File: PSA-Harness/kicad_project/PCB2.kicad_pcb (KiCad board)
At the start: 4 copper layers, 28.3 x 54 mm, 15 parts, among them J1 to_EPS_1, J2 to_EPS_2, J3 to_ESP_3, J7 USB_C_Receptacle, J8 B2B_1, J9 B2B_2, U1 DG419LEUA, U2 DG419LEUA

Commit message: use bom component names
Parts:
- D1, D2: value BAS40TW-AU -> BAS40SDW-AU_R1_000A1
- J7: value USB_C_Receptacle -> TYPE-C-31-M-07
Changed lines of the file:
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@@
 			)
 		)
-		(property "Value" "USB_C_Receptacle"
-			(at -0.6 -3.835 270)
+		(property "Value" "TYPE-C-31-M-07"
+			(at -0.6 -3.835 90)
 			(layer "F.Fab")
 			(effects
@@
 		(tags "SOT-363 SC-70-6 SC-88")
 		(property "Reference" "D1"
-			(at 0 2.03 270)
+			(at 0 2.03 90)
 			(layer "F.SilkS")
 			(effects
@@
 			)
 		)
-		(property "Value" "BAS40TW-AU"
-			(at 0 2 270)
+		(property "Value" "BAS40SDW-AU_R1_000A1"
+			(at 0 2 90)
 			(layer "F.Fab")
 			(effects
@@
 		)
 		(fp_text user "${REFERENCE}"
-			(at 0 0 180)
+			(at 0 0 0)
 			(layer "F.Fab")
 			(effects
@@
 			)
 		)
-		(property "Value" "BAS40TW-AU"
+		(property "Value" "BAS40SDW-AU_R1_000A1"
 			(at 0 2 90)
 			(layer "F.Fab")

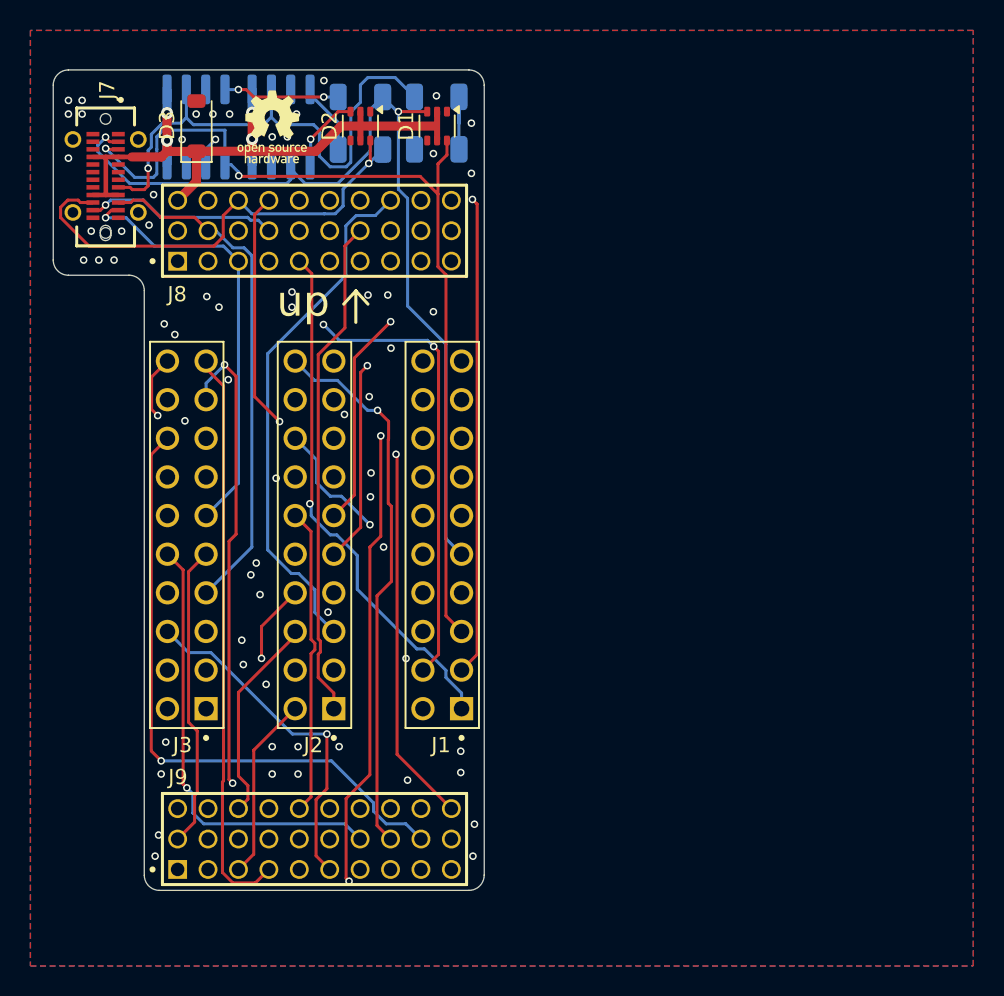
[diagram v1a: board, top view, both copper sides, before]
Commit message: move all psa harness components to top layer
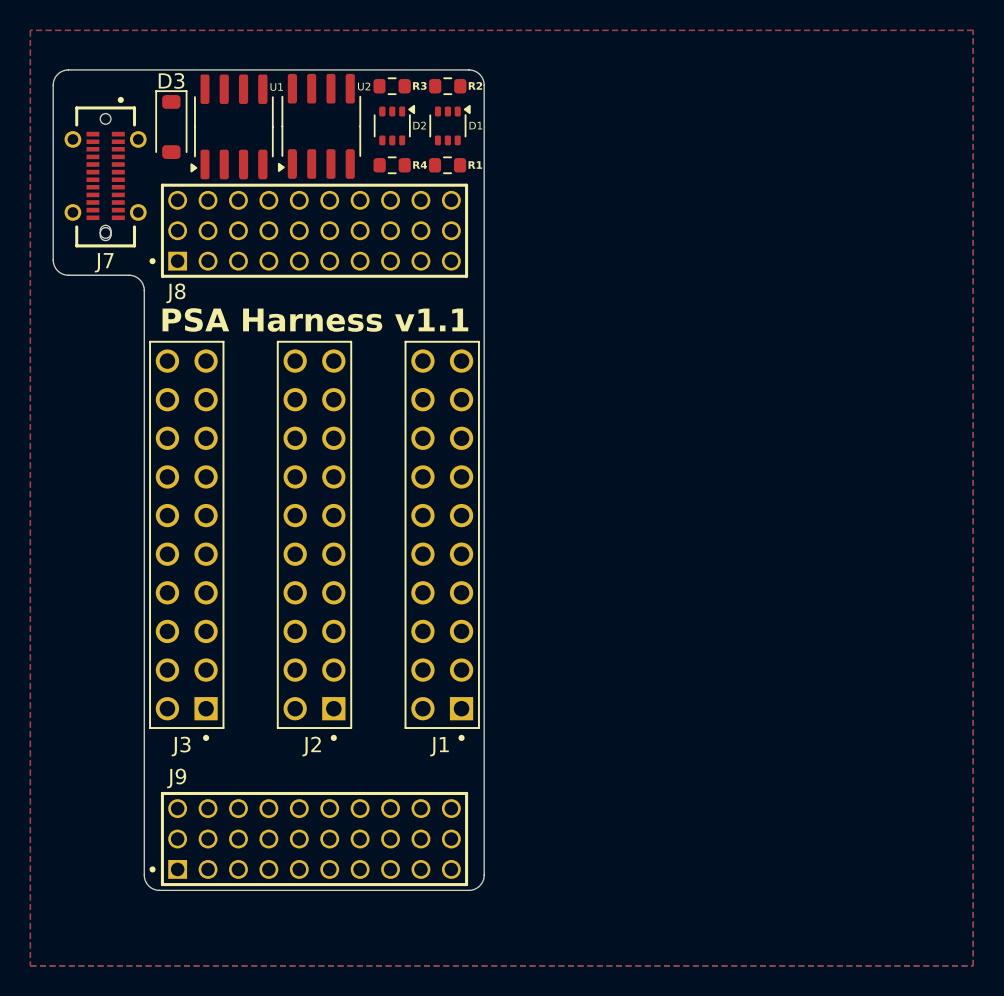
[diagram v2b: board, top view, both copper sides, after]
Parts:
- R1, R2, R3, R4: footprint Resistor_SMD:R_1206_3216Metric -> Resistor_SMD:R_0603_1608Metric; moved to F.Cu
- U1, U2: moved to F.Cu
- moved R1 5.82 mm to (114.4, 97.9), turned to 0 degrees
- moved R2 5.79 mm to (114.4, 92.7), turned to 180 degrees
- moved R4 3.11 mm to (110.8, 97.9), turned to 0 degrees
- moved R3 3.02 mm to (110.8, 92.7), turned to 180 degrees
- moved U2 2.65 mm to (106.1, 95.3)
- moved U1 2.49 mm to (100.4, 95.3)
- moved D2 2.10 mm to (110.8, 95.3)
- moved D3 1.65 mm to (96.3, 95.4), turned to -90 degrees
- moved D1 0.71 mm to (114.5, 95.3)
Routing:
- net +12V: track 81.5 -> 0.00 mm, vias 4 -> 0
- net CAN0_L: track 62.6 -> 0.00 mm, vias 2 -> 0
- net CAN0_H: track 61.6 -> 0.00 mm, vias 2 -> 0
- net 59: track 47.6 -> 0.00 mm, vias 1 -> 0
- net 60: track 47.4 -> 0.00 mm, vias 2 -> 0
- net 28: track 45.3 -> 0.00 mm, vias 2 -> 0
- net 2: track 43.6 -> 0.00 mm, vias 1 -> 0
- net 12: track 42.1 -> 0.00 mm, vias 2 -> 0
- net 58: track 41.5 -> 0.00 mm, vias 1 -> 0
- net 30: track 38.2 -> 0.00 mm, vias 1 -> 0
- net 56: track 38.0 -> 0.00 mm, vias 1 -> 0
- net CAN2_L: track 38.0 -> 0.00 mm, vias 2 -> 0
- net 50: track 37.8 -> 0.00 mm
- net SBU1: track 37.2 -> 0.00 mm, vias 1 -> 0
- net 29: track 36.2 -> 0.00 mm, vias 1 -> 0
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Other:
- board text added: "PSA Harness v1.1"
- board text removed: "up"

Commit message: CAN signals routed
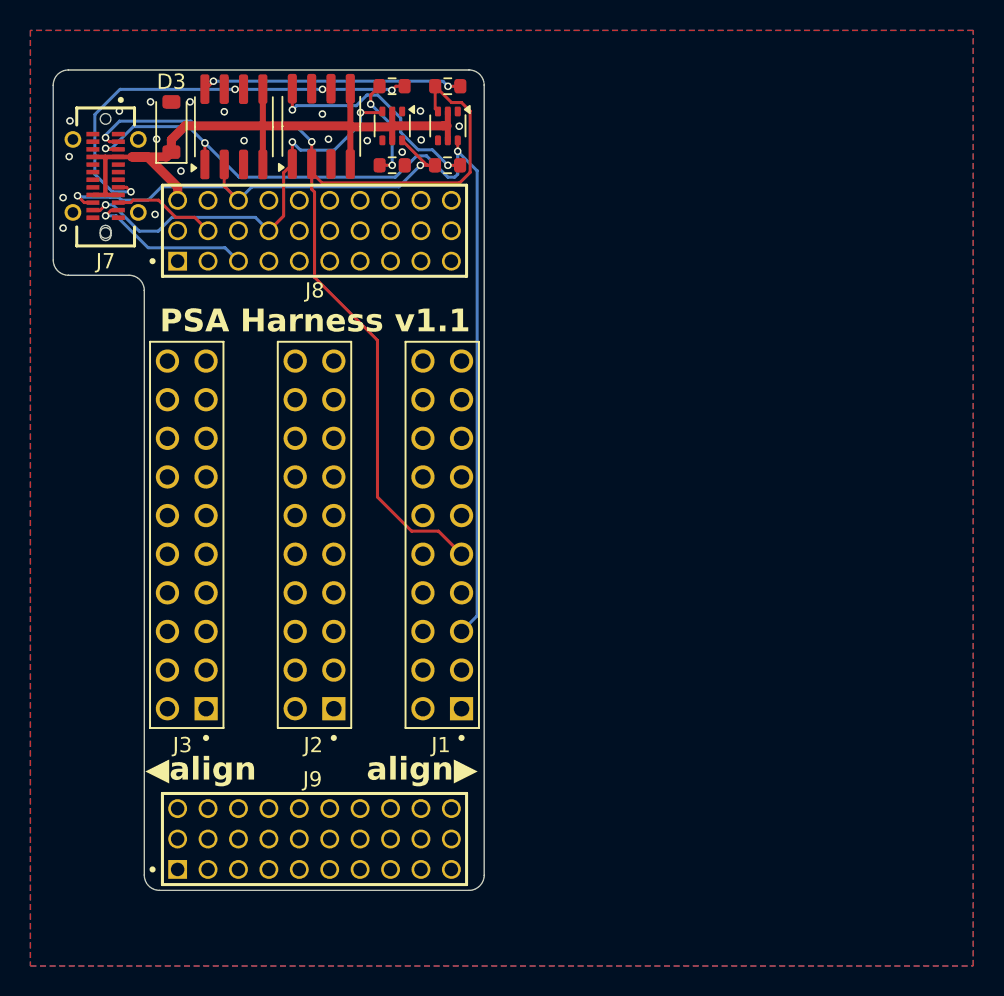
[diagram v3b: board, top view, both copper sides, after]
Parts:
- turned D3 to 90 degrees
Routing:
- net CAN0_H: track 0.00 -> 68.0 mm, vias 0 -> 2
- net CAN0_L: track 0.00 -> 63.4 mm, vias 0 -> 3
- net +12V: track 0.00 -> 47.3 mm
- net CAN2_L: track 0.00 -> 32.1 mm, vias 0 -> 2
- net SBU1: track 0.00 -> 30.1 mm, vias 0 -> 4
- net CAN2_H: track 0.00 -> 27.3 mm, vias 0 -> 3
- net Net-(R2-Pad1): track 0.00 -> 17.2 mm, vias 0 -> 2
- net Net-(R1-Pad2): track 0.00 -> 15.3 mm, vias 0 -> 2
- net CAN1_H: track 0.00 -> 11.0 mm, vias 0 -> 1
- net Net-(R3-Pad2): track 0.00 -> 6.85 mm, vias 0 -> 2
- net CAN1_L: track 0.00 -> 6.80 mm
- net GND: vias 0 -> 19
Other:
- board text added: "align▶"
- board text added: "◀align"

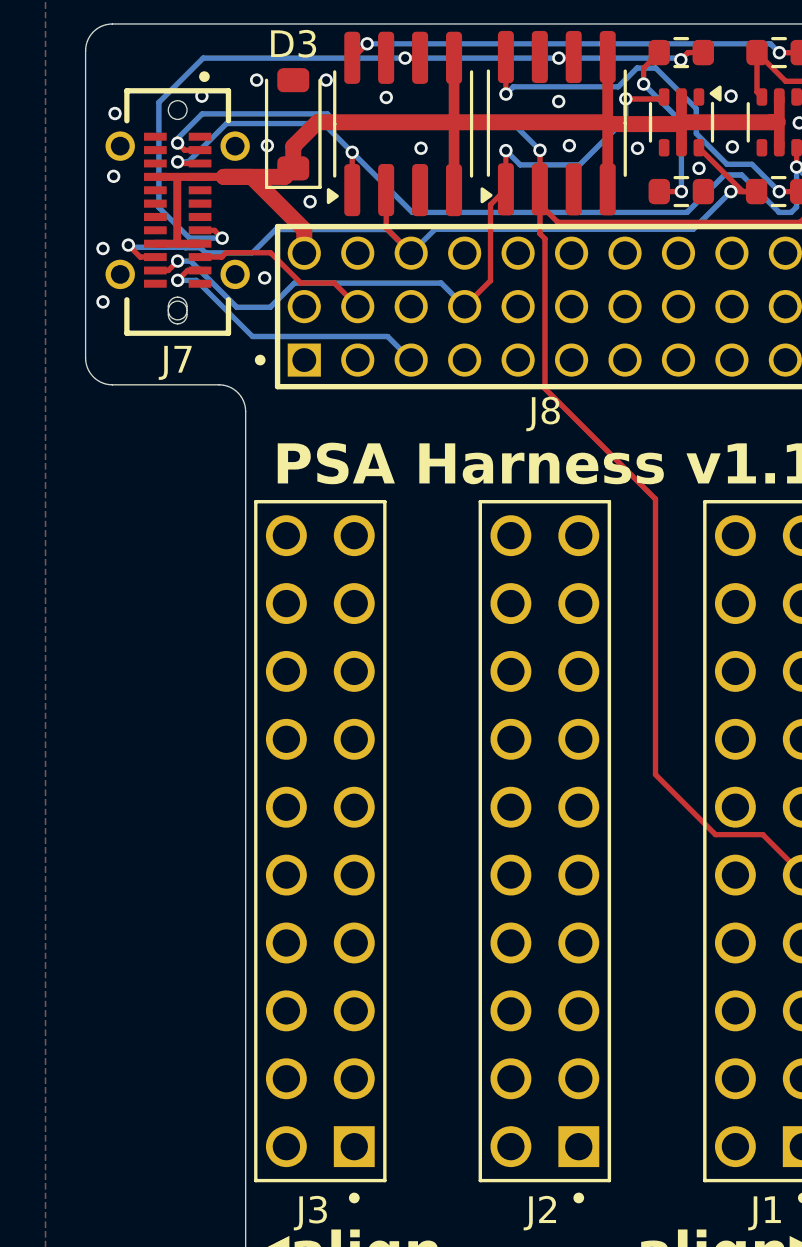
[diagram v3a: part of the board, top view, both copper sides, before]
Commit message: routed power
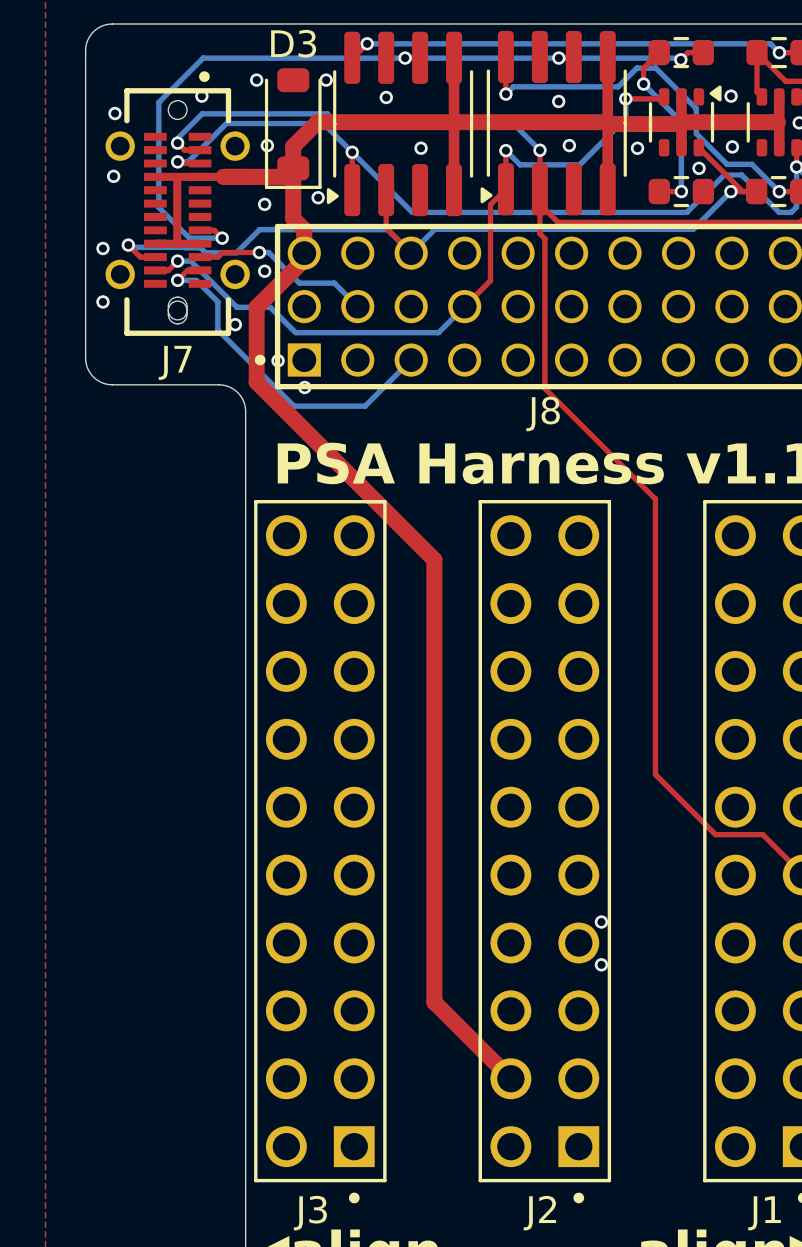
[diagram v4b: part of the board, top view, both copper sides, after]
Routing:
- net +12V: track 47.3 -> 82.6 mm
- net CAN1_H: track 11.0 -> 13.0 mm
- net CAN1_L: track 6.80 -> 6.81 mm, vias 0 -> 1
- net GND: vias 19 -> 25

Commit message: pcb2 routed
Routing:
- net 59: track 0.00 -> 51.7 mm
- net 21: track 0.00 -> 44.1 mm, vias 0 -> 2
- net 2: track 0.00 -> 43.5 mm, vias 0 -> 1
- net 60: track 0.00 -> 43.0 mm, vias 0 -> 1
- net 58: track 0.00 -> 39.5 mm, vias 0 -> 1
- net 12: track 0.00 -> 39.0 mm, vias 0 -> 1
- net 28: track 0.00 -> 38.4 mm, vias 0 -> 1
- net 40: track 0.00 -> 38.3 mm, vias 0 -> 2
- net 14: track 0.00 -> 37.8 mm, vias 0 -> 2
- net 30: track 0.00 -> 37.8 mm, vias 0 -> 1
- net 50: track 0.00 -> 37.5 mm, vias 0 -> 1
- net 57: track 0.00 -> 36.5 mm, vias 0 -> 1
- net 29: track 0.00 -> 35.6 mm, vias 0 -> 1
- net 56: track 0.00 -> 35.5 mm, vias 0 -> 1
- net 1: track 0.00 -> 34.1 mm
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
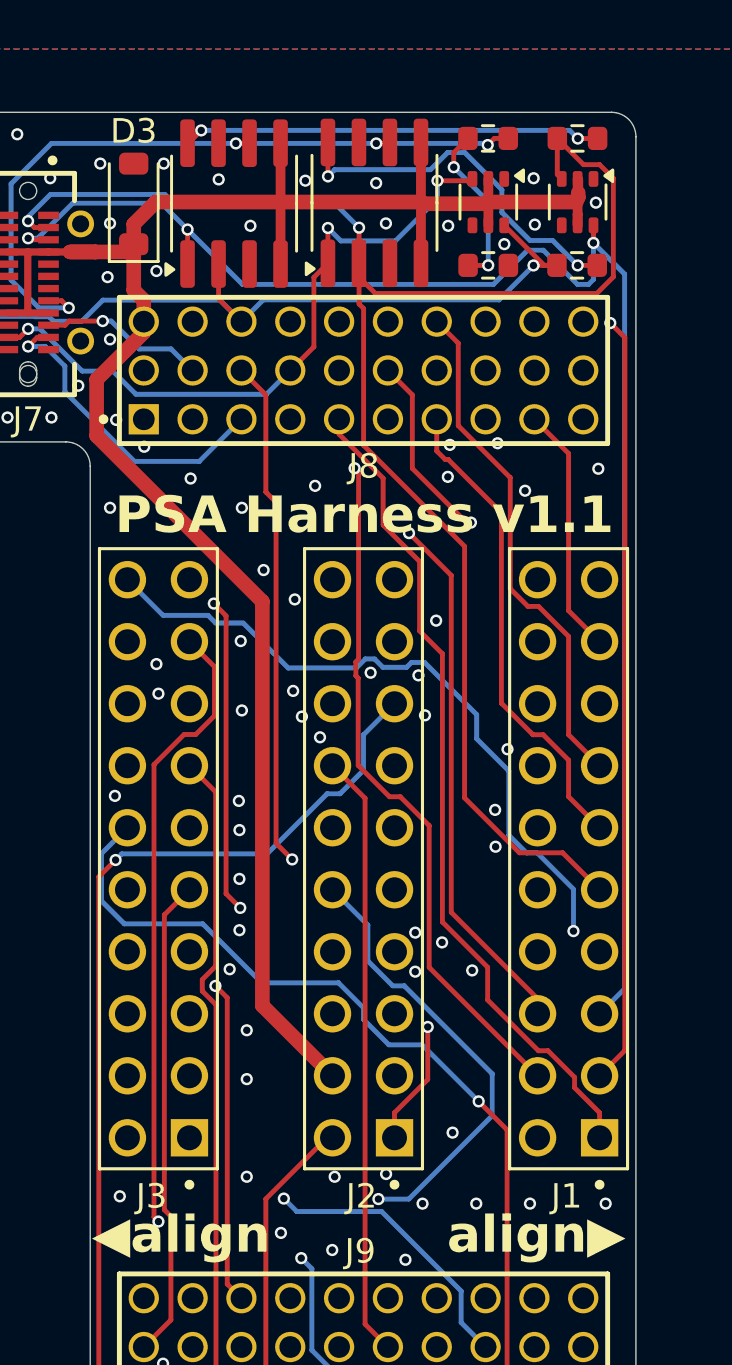
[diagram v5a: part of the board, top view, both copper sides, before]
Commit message: pcb2 fixed drc
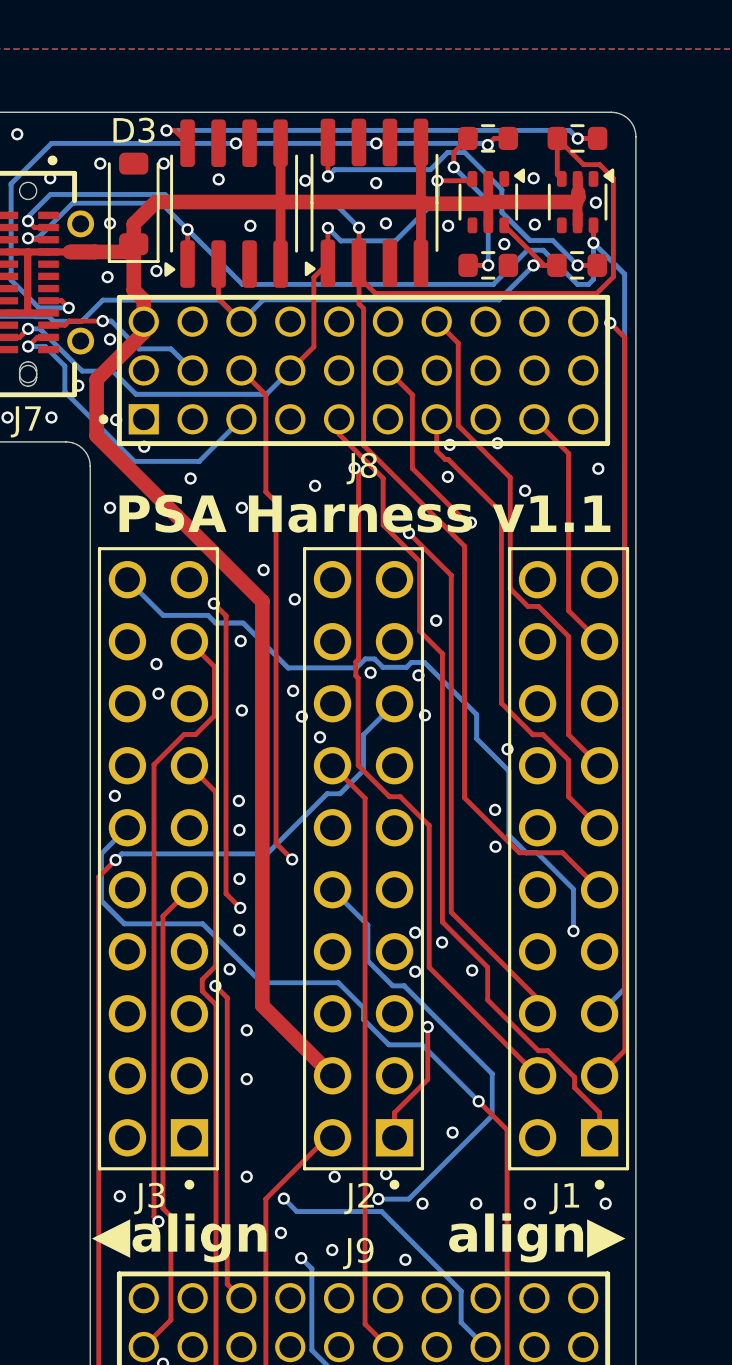
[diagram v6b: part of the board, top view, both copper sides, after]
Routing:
- net Net-(R2-Pad1): track 17.2 -> 18.9 mm
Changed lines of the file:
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@@
 	)
 	(segment
-		(start 98.511 92.865)
-		(end 99.035 92.341)
+		(start 97.956 92.346)
+		(end 97.61 92.346)
+		(width 0.2)
+		(layer "F.Cu")
+		(net 21)
+	)
+	(segment
+		(start 98.475 92.865)
+		(end 97.956 92.346)
 		(width 0.2)
 		(layer "F.Cu")
@@
 	)
 	(via
-		(at 99.035 92.341)
+		(at 97.61 92.346)
 		(size 0.5)
 		(drill 0.3)
@@
 	)
 	(segment
-		(start 99.035 92.341)
+		(start 97.61 92.346)
+		(end 97.615 92.341)
+		(width 0.2)
+		(layer "B.Cu")
+		(net 21)
+	)
+	(segment
+		(start 97.615 92.341)
 		(end 114.125 92.341)
 		(width 0.2)
@@
 	)
 	(segment
+		(start 97.471 116.905)
+		(end 98.552 115.824)
+		(width 0.2)
+		(layer "In2.Cu")
+		(net 52)
+	)
+	(segment
 		(start 98.682 140.174)
 		(end 98.682 137.7116)
@@
 	)
 	(segment
-		(start 97.5231 136.5527)
-		(end 97.5231 116.8529)
+		(start 97.471 136.5006)
+		(end 97.471 116.905)
 		(width 0.2)
 		(layer "In2.Cu")
@@
 	(segment
 		(start 98.682 137.7116)
-		(end 97.5231 136.5527)
-		(width 0.2)
-		(layer "In2.Cu")
-		(net 52)
-	)
-	(segment
-		(start 97.5231 116.8529)
-		(end 98.552 115.824)
+		(end 97.471 136.5006)
 		(width 0.2)
 		(layer "In2.Cu")
@@
 	)
 	(segment
-		(start 97.5238 124.4722)
-		(end 98.552 123.444)
-		(width 0.2)
-		(layer "F.Cu")
-		(net 59)
-	)
-	(segment
-		(start 97.7935 136.8231)
-		(end 97.5238 136.5534)
-		(width 0.2)
-		(layer "F.Cu")
-		(net 59)
-	)
-	(segment
-		(start 97.5238 136.5534)
-		(end 97.5238 124.4722)
-		(width 0.2)
-		(layer "F.Cu")
-		(net 59)
-	)
-	(segment
 		(start 96.682 142.174)
 		(end 97.7935 141.0625)
@@
 	)
 	(segment
+		(start 97.468 124.528)
+		(end 98.552 123.444)
+		(width 0.2)
+		(layer "F.Cu")
+		(net 59)
+	)
+	(segment
+		(start 97.468 136.4976)
+		(end 97.468 124.528)
+		(width 0.2)
+		(layer "F.Cu")
+		(net 59)
+	)
+	(segment
 		(start 97.7935 141.0625)
 		(end 97.7935 136.8231)
 		(width 0.2)
 		(layer "F.Cu")
+		(net 59)
+	)
+	(segment
+		(start 97.7935 136.8231)
+		(end 97.468 136.4976)
+		(width 0.2)
+		(layer "F.Cu")

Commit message: change pcb2 to jlc parts
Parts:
- D3: value SMF16A -> C353308
- J1: value to_EPS_1 -> PH-01481
- J2: value to_EPS_2 -> PH-01481
- J3: value to_ESP_3 -> PH-01481
- R1, R2, R3, R4: value 120R -> CRCW0603120RFKEAHP
- U1, U2: value DG419LEUA -> DG419LEDY-T1-GE4
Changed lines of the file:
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@@
 			)
 		)
-		(property "Value" "to_ESP_3"
+		(property "Value" "PH-01481"
 			(at 13.774 0.918 180)
 			(layer "F.Fab")
@@
 			)
 		)
-		(property "Value" "120R"
+		(property "Value" "CRCW0603120RFKEAHP"
 			(at 0 1.43 0)
 			(layer "F.Fab")
@@
 			)
 		)
-		(property "Description" ""
+		(property "Description" "120R"
 			(at 0 0 0)
 			(layer "F.Fab")
@@
 			)
 		)
-		(property "Value" "SMF16A"
+		(property "Value" "C353308"
 			(at 0 2.1 90)
 			(layer "F.Fab")
@@
 			)
 		)
-		(property "Description" "200W unidirectional Transil Transient Voltage Suppressor, 16Vrwm, SMF"
+		(property "Description" "SMF16A - 200W unidirectional Transil Transient Voltage Suppressor, 16Vrwm, SMF"
 			(at 0 0 90)
 			(unlocked yes)
@@
 			)
 		)
-		(property "Value" "120R"
+		(property "Value" "CRCW0603120RFKEAHP"
 			(at 0 1.43 0)
 			(layer "F.Fab")
@@
 			)
 		)
-		(property "Description" ""
+		(property "Description" "120R"
 			(at 0 0 0)
 			(layer "F.Fab")
@@
 			)
 		)
-		(property "Value" "120R"
+		(property "Value" "CRCW0603120RFKEAHP"
 			(at 0 1.43 0)
 			(layer "F.Fab")
@@
 			)
 		)
-		(property "Description" ""
+		(property "Description" "120R"
 			(at 0 0 0)
 			(layer "F.Fab")
@@
 			)
 		)
-		(property "Value" "to_EPS_2"
+		(property "Value" "PH-01481"
 			(at 13.774 0 180)
 			(layer "F.Fab")
@@
 			)
 		)
-		(property "Value" "DG419LEUA"
+		(property "Value" "DG419LEDY-T1-GE4"
 			(at 0 3.4 90)
 			(layer "F.Fab")
@@
 			)
 		)
-		(property "Value" "120R"
+		(property "Value" "CRCW0603120RFKEAHP"
 			(at 0 1.43 0)
 			(layer "F.Fab")
@@
 			)
 		)
-		(property "Description" ""
+		(property "Description" "120R"
 			(at 0 0 0)
 			(layer "F.Fab")
@@
 			)
 		)
-		(property "Value" "to_EPS_1"
+		(property "Value" "PH-01481"
 			(at 13.774 -0.882 180)
 			(layer "F.Fab")
@@
 			)
 		)
-		(property "Value" "DG419LEUA"
+		(property "Value" "DG419LEDY-T1-GE4"
 			(at 0 3.4 90)
 			(layer "F.Fab")
